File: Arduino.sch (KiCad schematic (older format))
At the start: 0 parts

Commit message: Module 3, Unit 9: Understanding The Arduino Module
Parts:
- added ARD?: ARDUINOPINS, symbol ARDUINOPINS
- added R? (x13): R, symbol R
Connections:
- net MISO: now also R?.2
- net MOSI: now also R?.2
- net SCLK: now also R?.2
- net TACH_MEAS: now also R?.1
- new net: ARD?.11 (Digital0), R?.1
- new net: ARD?.12 (Digital1), R?.1
- new net: ARD?.8 (AnalogIn3), R?.2
- new net: ARD?.7 (AnalogIn2), R?.2
- new net: ARD?.6 (AnalogIn1), R?.2
- new net: ARD?.5 (AnalogIn0), R?.2
- new net: ARD?.21 (CS_N), R?.1
- new net: ARD?.22 (MOSI), R?.1
- new net: ARD?.23 (MISO), R?.1
- new net: ARD?.24 (SCK), R?.1
- new net: ARD?.20 (PWM0), R?.1
- new net: ARD?.19 (Digital8), R?.1
- new net ADC_CS_N: R?.2
- new net CURR_MEAS: R?.1
- new net DAC_CS_N: R?.2
- new net FAN_EN_N: R?.2
- new net GND: R?.1
- new net LED_EN_PWM: R?.2
- new net RELAY+: R?.2
- new net RELAY-: R?.2
- new net V+_ADJ_MON: R?.1
- new net V-_ADJ_MON: R?.1

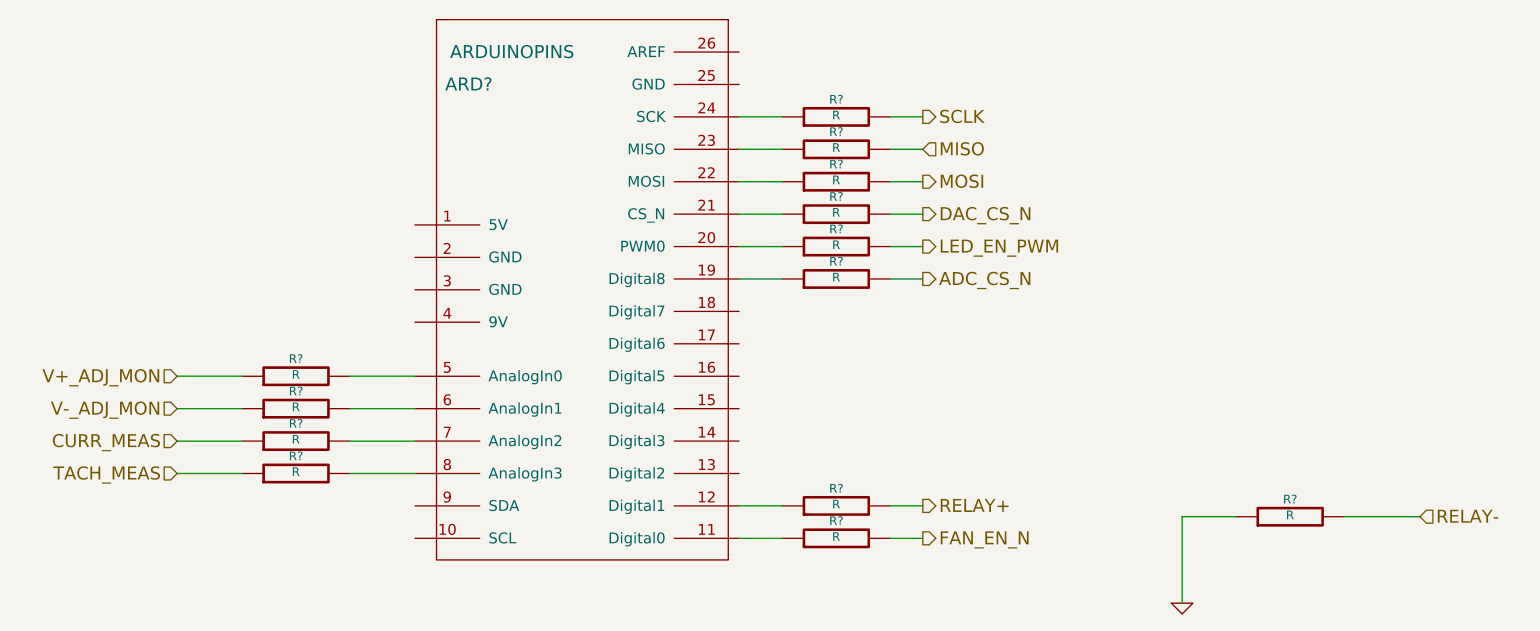
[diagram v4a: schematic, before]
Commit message: Module 3, Unit 10: Revisiting The Current/Fan Module
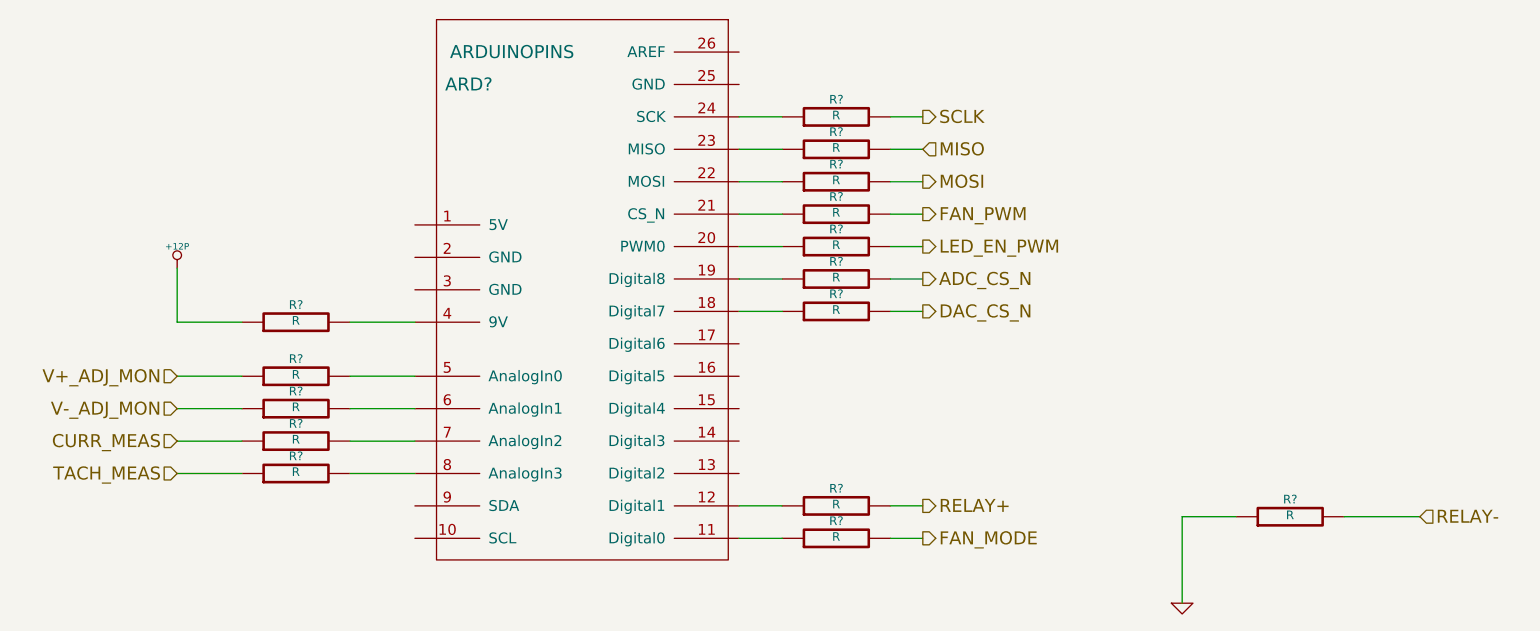
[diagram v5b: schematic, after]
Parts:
- added R? (x2): R, symbol R
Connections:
- net at R?.1: now also ARD?.21 (CS_N); no longer ARD?.11 (Digital0)
- net at R?.1: now also ARD?.18 (Digital7); no longer ARD?.21 (CS_N)
- net at ARD?.4 (9V): now also R?.2
- net FAN_EN_N renamed FAN_PWM
- new net: ARD?.11 (Digital0), R?.1
- new net +12P: R?.1
- new net FAN_MODE: R?.2
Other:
- moved on the sheet: R?
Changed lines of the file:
@@
 Text HLabel 5800 2300 2    60   Output ~ 0
 SCLK
+Text HLabel 5800 3200 2    60   Output ~ 0
+DAC_CS_N
 Text HLabel 5800 2750 2    60   Output ~ 0
-DAC_CS_N
-Text HLabel 5800 4250 2    60   Output ~ 0
-FAN_EN_N
+FAN_PWM
 Text HLabel 2350 3950 0    60   Input ~ 0
 TACH_MEAS
@@
 L R R?
 U 1 1 5302FBB6
-P 5400 4250
-F 0 "R?" V 5480 4250 40  0000 C CNN
-F 1 "R" V 5407 4251 40  0000 C CNN
-F 2 "" V 5330 4250 30  0000 C CNN
-F 3 "" H 5400 4250 30  0000 C CNN
-	1    5400 4250
-	0    -1   -1   0
-$EndComp
-Wire Wire Line
-	5150 4250 4950 4250
-Wire Wire Line
-	5650 4250 5800 4250
+P 5400 2750
+F 0 "R?" V 5480 2750 40  0000 C CNN
+F 1 "R" V 5407 2751 40  0000 C CNN
+F 2 "" V 5330 2750 30  0000 C CNN
+F 3 "" H 5400 2750 30  0000 C CNN
+	1    5400 2750
+	0    -1   -1   0
+$EndComp
+Wire Wire Line
+	5150 2750 4950 2750
+Wire Wire Line
+	5650 2750 5800 2750
 $Comp
 L R R?
@@
 L R R?
 U 1 1 53030B8B
-P 5400 2750
-F 0 "R?" V 5480 2750 40  0000 C CNN
-F 1 "R" V 5407 2751 40  0000 C CNN
-F 2 "" V 5330 2750 30  0000 C CNN
-F 3 "" H 5400 2750 30  0000 C CNN
-	1    5400 2750
+P 5400 3200
+F 0 "R?" V 5480 3200 40  0000 C CNN
+F 1 "R" V 5407 3201 40  0000 C CNN
+F 2 "" V 5330 3200 30  0000 C CNN
+F 3 "" H 5400 3200 30  0000 C CNN
+	1    5400 3200
 	0    -1   -1   0
 $EndComp
@@
 	5150 2900 4950 2900
 Wire Wire Line
-	4950 2750 5150 2750
+	4950 3200 5150 3200
 Wire Wire Line
 	5150 2600 4950 2600
@@
 	5650 2600 5800 2600
 Wire Wire Line
-	5800 2750 5650 2750
+	5800 3200 5650 3200
 Wire Wire Line
 	5650 2900 5800 2900
@@
 Wire Wire Line
 	5150 3050 4950 3050
+Text HLabel 5800 4250 2    60   Output ~ 0
+FAN_MODE
+$Comp
+L R R?
+U 1 1 5302FC7C
+P 5400 4250
+F 0 "R?" V 5480 4250 40  0000 C CNN
+F 1 "R" V 5407 4251 40  0000 C CNN
+F 2 "" V 5330 4250 30  0000 C CNN
+F 3 "" H 5400 4250 30  0000 C CNN
+	1    5400 4250
+	0    -1   -1   0
+$EndComp
+Wire Wire Line
+	5650 4250 5800 4250
+Wire Wire Line
+	5150 4250 4950 4250
+$Comp
+L R R?
+U 1 1 5302FCC2
+P 2900 3250
+F 0 "R?" V 2980 3250 40  0000 C CNN
+F 1 "R" V 2907 3251 40  0000 C CNN
+F 2 "" V 2830 3250 30  0000 C CNN
+F 3 "" H 2900 3250 30  0000 C CNN
+	1    2900 3250
+	0    -1   -1   0
+$EndComp
+Wire Wire Line
+	3150 3250 3450 3250
+$Comp
+L +12P #PWR?
+U 1 1 5302FCEE
+P 2350 3000
+F 0 "#PWR?" H 2350 2970 30  0001 C CNN
+F 1 "+12P" H 2350 3100 30  0000 C CNN
+F 2 "" H 2350 3000 60  0000 C CNN
+F 3 "" H 2350 3000 60  0000 C CNN
+	1    2350 3000
+	1    0    0    -1
+$EndComp
+Wire Wire Line
+	2350 3000 2350 3250
+Wire Wire Line
+	2350 3250 2650 3250
 $EndSCHEMATC
